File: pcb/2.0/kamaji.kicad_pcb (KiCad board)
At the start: 2 copper layers, 100 x 100 mm, 83 parts, among them J1 RJ10, J2 RJ10, J3 RJ10, J4 RJ10, J5 RJ10, J6 RJ10, J7 USB_B, J8 USB_A, Q1 2N3904, Q2 IRL540N, Q3 IRL540N, SW1 SW_Push, SW2 SW_Push, SW3 SW_Push, U1 ATMEGA32U4-AU, Y1 16MHz

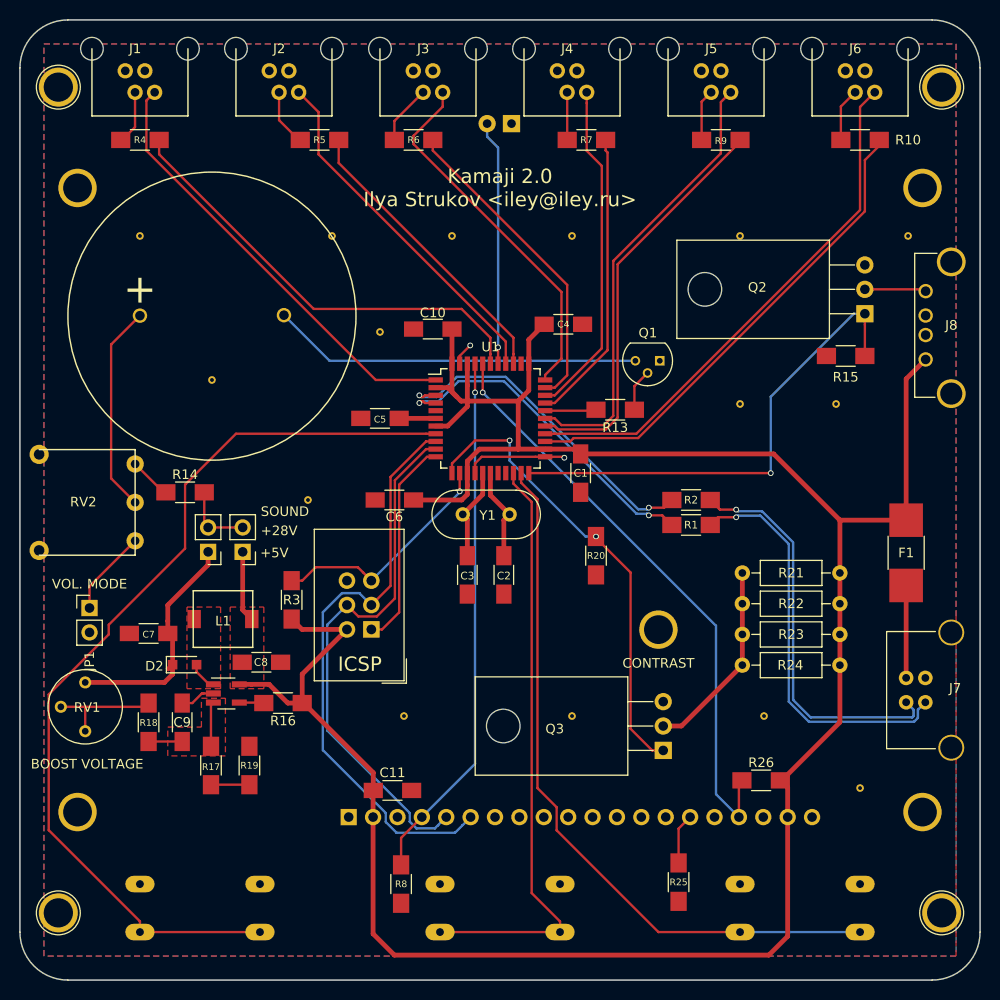
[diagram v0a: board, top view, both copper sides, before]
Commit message: fix a couple of silkscreen labels
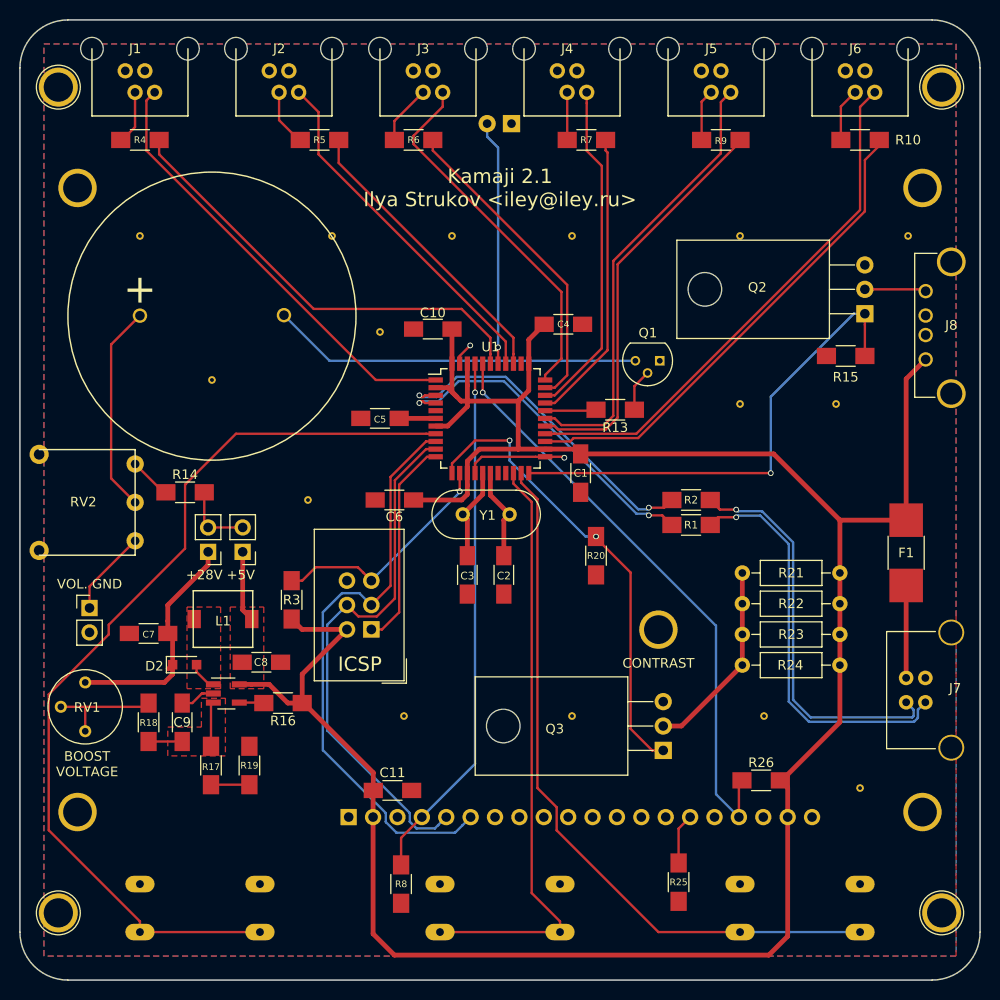
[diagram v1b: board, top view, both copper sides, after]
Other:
- board text added: "Kamaji 2.1 Ilya Strukov <iley@iley.ru>"
- board text added: "VOL. GND"
- board text removed: "Kamaji 2.0 Ilya Strukov <iley@iley.ru>"
- board text removed: "SOUND"
- board text removed: "VOL. MODE"
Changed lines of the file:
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@@
     (area 46.224999 46.55 157.775001 150.075001)
     (thickness 1.6)
-    (drawings 16)
+    (drawings 15)
     (tracks 378)
     (zones 0)
@@
     (descr "Through hole straight pin header, 1x02, 2.54mm pitch, single row")
     (tags "Through hole pin header THT 1x02 2.54mm single row")
-    (fp_text reference JP1 (at 0 5.54 90) (layer F.SilkS)
+    (fp_text reference JP1 (at -2.45 0.95 90) (layer F.SilkS) hide
       (effects (font (size 1 1) (thickness 0.15)))
     )
@@
     (effects (font (size 1 1) (thickness 0.2)))
   )
-  (gr_text "BOOST VOLTAGE" (at 57 127.5) (layer F.SilkS)
+  (gr_text "BOOST\nVOLTAGE" (at 57 127.5) (layer F.SilkS)
     (effects (font (size 1 1) (thickness 0.2)))
   )
-  (gr_text "VOL. MODE" (at 57.25 108.75) (layer F.SilkS)
-    (effects (font (size 1 1) (thickness 0.2)))
-  )
-  (gr_text SOUND (at 77.6 101.2) (layer F.SilkS)
+  (gr_text "VOL. GND" (at 57.25 108.75) (layer F.SilkS)
     (effects (font (size 1 1) (thickness 0.2)))
   )
@@
     (effects (font (size 1.5 1.5) (thickness 0.3)))
   )
-  (gr_text +5V (at 76.5 105.5) (layer F.SilkS)
+  (gr_text +5V (at 73 107.8) (layer F.SilkS)
     (effects (font (size 1 1) (thickness 0.2)))
   )
-  (gr_text +28V (at 77 103.2) (layer F.SilkS)
+  (gr_text +28V (at 69.2 107.8) (layer F.SilkS)
     (effects (font (size 1 1) (thickness 0.2)))
   )
-  (gr_text "Kamaji 2.0\nIlya Strukov <iley@iley.ru>" (at 100 67.5) (layer F.SilkS)
+  (gr_text "Kamaji 2.1\nIlya Strukov <iley@iley.ru>" (at 100 67.5) (layer F.SilkS)
     (effects (font (size 1.5 1.5) (thickness 0.25)))
   )

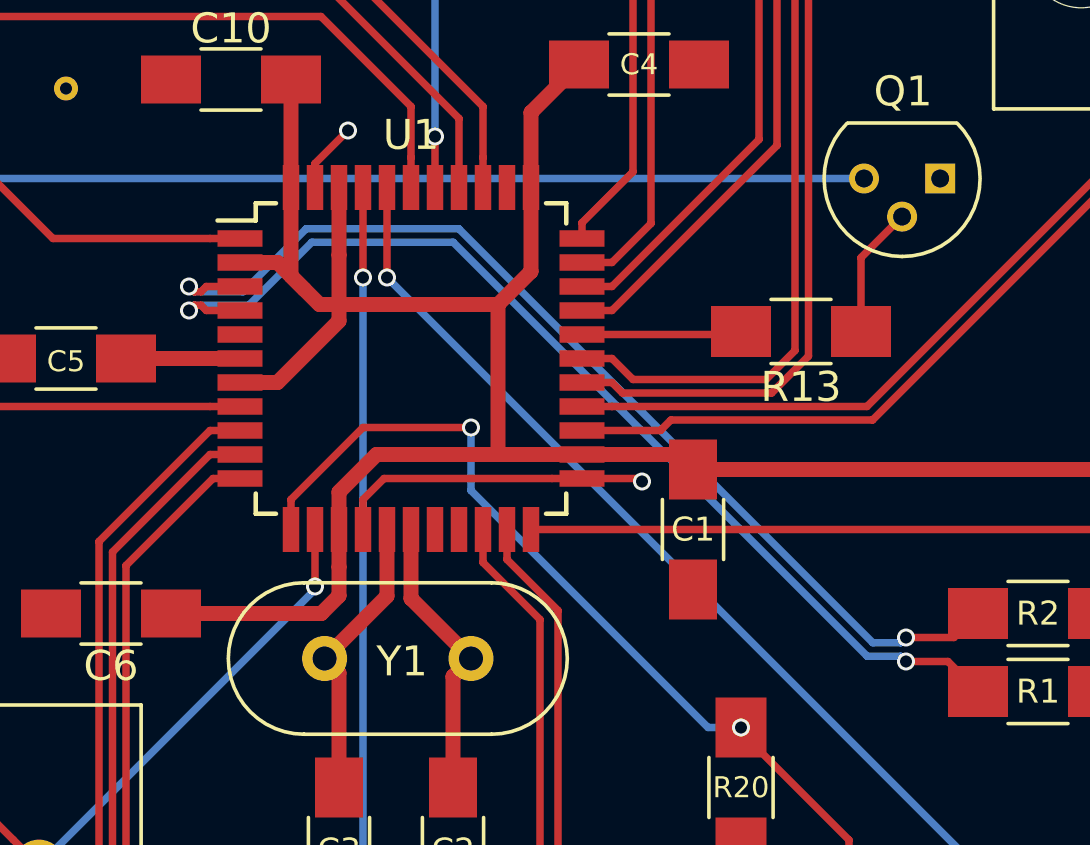
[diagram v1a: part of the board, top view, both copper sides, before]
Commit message: move a couple of tracks
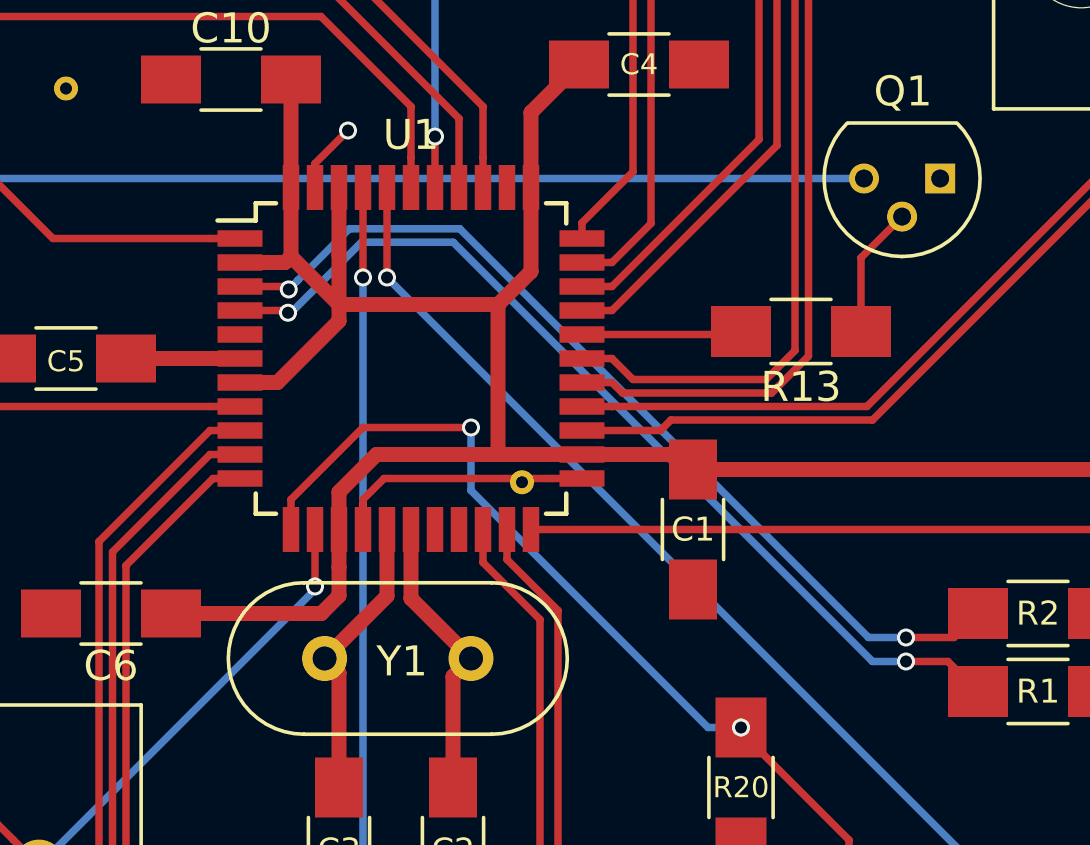
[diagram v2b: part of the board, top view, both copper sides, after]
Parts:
- added VIA**: Via_0.8mm, kamaji:Via_0.8mm, F.Cu at (102.7, 95.6)
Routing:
- net /USB_D-: track 35.2 -> 31.5 mm
- net /USB_D+: track 35.3 -> 31.8 mm
- net GND: track 16.7 -> 14.6 mm, vias 2 -> 1
- net VCC: track 264.2 -> 263.1 mm
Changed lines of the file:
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@@
 (kicad_pcb (version 4) (host pcbnew 4.0.7)
   (general
-    (links 178)
+    (links 179)
     (no_connects 0)
     (area 46.224999 46.55 157.775001 150.075001)
     (thickness 1.6)
     (drawings 15)
-    (tracks 378)
+    (tracks 365)
     (zones 0)
-    (modules 83)
+    (modules 84)
     (nets 57)
   )
@@
   )
   (module kamaji:Via_0.8mm (layer F.Cu)
+    (at 102.7 95.625)
+    (fp_text reference VIA** (at 0 1.5) (layer F.SilkS) hide
+      (effects (font (size 1 1) (thickness 0.15)))
+    )
+    (fp_text value Via_0.8mm (at 0 -1.5) (layer F.Fab) hide
+      (effects (font (size 1 1) (thickness 0.15)))
+    )
+    (pad 1 thru_hole circle (at 0 0) (size 0.8 0.8) (drill 0.4) (layers *.Cu *.Mask)
+      (net 49 GND) (zone_connect 2))
+  )
+  (module kamaji:Via_0.8mm (layer F.Cu)
     (at 80 100)
     (fp_text reference VIA** (at 0 1.5) (layer F.SilkS) hide
@@
   (segment (start 72.85 121.1) (end 75.35 121.1) (width 0.25) (layer F.Cu) (net 2))
   (segment (start 75.35 121.1) (end 75.4 121.15) (width 0.25) (layer F.Cu) (net 2))
+  (segment (start 96.6 89.7) (end 95 88.1) (width 0.5) (layer F.Cu) (net 3))
+  (segment (start 95 88.1) (end 94.8 88.3) (width 0.5) (layer F.Cu) (net 3))
+  (segment (start 94.8 88.3) (end 93.3 88.3) (width 0.5) (layer F.Cu) (net 3))
+  (segment (start 95 88.1) (end 95 85.8) (width 0.5) (layer F.Cu) (net 3))
+  (segment (start 101.9 89.7) (end 96.6 89.7) (width 0.5) (layer F.Cu) (net 3))
   (segment (start 129.961034 133.024284) (end 129.961034 145.438966) (width 0.5) (layer F.Cu) (net 3))
   (segment (start 129.961034 145.438966) (end 128 147.4) (width 0.5) (layer F.Cu) (net 3))
@@
   (segment (start 94.55 92.3) (end 96.6 90.25) (width 0.5) (layer F.Cu) (net 3))
   (segment (start 96.6 90.25) (end 96.6 89.7) (width 0.5) (layer F.Cu) (net 3))
-  (segment (start 101.9 89.7) (end 96.6 89.7) (width 0.5) (layer F.Cu) (net 3))
-  (segment (start 96.6 89.7) (end 95.95 89.7) (width 0.5) (layer F.Cu) (net 3))
-  (segment (start 95.95 89.7) (end 95.45 89.2) (width 0.5) (layer F.Cu) (net 3))
   (segment (start 96.6 99.410002) (end 96.6 98.45) (width 0.5) (layer F.Cu) (net 3))
   (segment (start 96.6 98.45) (end 96.6 97.2) (width 0.5) (layer F.Cu) (net 3))
@@
   (segment (start 103 85.8) (end 103 83.3) (width 0.5) (layer F.Cu) (net 3))
   (segment (start 103 83.3) (end 104.6 81.7) (width 0.5) (layer F.Cu) (net 3))
-  (segment (start 95.45 89.2) (end 95 88.75) (width 0.5) (layer F.Cu) (net 3))
-  (segment (start 95 88.75) (end 95 85.8) (width 0.5) (layer F.Cu) (net 3))
-  (segment (start 94.55 88.3) (end 93.3 88.3) (width 0.5) (layer F.Cu) (net 3))
-  (segment (start 95.45 89.2) (end 94.55 88.3) (width 0.5) (layer F.Cu) (net 3))
   (segment (start 97.85 94.7) (end 96.6 95.95) (width 0.5) (layer F.Cu) (net 3))
   (segment (start 96.6 95.95) (end 96.6 97.2) (width 0.5) (layer F.Cu) (net 3))
@@
   (segment (start 96.6 101.98) (end 96.12 101.5) (width 0.5) (layer F.Cu) (net 5))
   (segment (start 89.5 91.5) (end 93.3 91.5) (width 0.5) (layer F.Cu) (net 6))
-  (via (at 97.4 88.8) (size 0.6) (drill 0.4) (layers F.Cu B.Cu) (net 7))
-  (segment (start 97.4 85.8) (end 97.4 88.8) (width 0.25) (layer F.Cu) (net 7))
-  (segment (start 97.4 127.485318) (end 91.861034 133.024284) (width 0.25) (layer B.Cu) (net 7))
   (segment (start 97.4 88.8) (end 97.4 127.485318) (width 0.25) (layer B.Cu) (net 7))
+  (segment (start 97.4 127.485318) (end 91.861034 133.024284) (width 0.25) (layer B.Cu) (net 7))
+  (segment (start 97.4 85.8) (end 97.4 88.8) (width 0.25) (layer F.Cu) (net 7))
+  (via (at 97.4 88.8) (size 0.6) (drill 0.4) (layers F.Cu B.Cu) (net 7))
   (segment (start 91.861034 133.024284) (end 89.7 135.185318) (width 0.25) (layer F.Cu) (net 7))
   (segment (start 89.7 135.185318) (end 89.7 138) (width 0.25) (layer F.Cu) (net 7))
@@
   (segment (start 118.6 134.225318) (end 119.801034 133.024284) (width 0.25) (layer F.Cu) (net 10))
   (segment (start 98.2 88.8) (end 98.2 85.8) (width 0.25) (layer F.Cu) (net 11))
-  (segment (start 124.881034 133.024284) (end 122.5 130.64325) (width 0.25) (layer B.Cu) (net 11))
-  (segment (start 122.5 130.64325) (end 122.5 113.1) (width 0.25) (layer B.Cu) (net 11))
   (segment (start 122.5 113.1) (end 98.2 88.8) (width 0.25) (layer B.Cu) (net 11))
+  (segment (start 122.5 130.64325) (end 122.5 113.1) (width 0.25) (layer B.Cu) (net 11))
+  (segment (start 124.881034 133.024284) (end 122.5 130.64325) (width 0.25) (layer B.Cu) (net 11))
   (via (at 98.2 88.8) (size 0.6) (drill 0.4) (layers F.Cu B.Cu) (net 11))
   (segment (start 124.881034 133.024284) (end 124.881034 129.518966) (width 0.25) (layer F.Cu) (net 11))
@@
   (segment (start 79.4 108.4) (end 80.8 107) (width 0.25) (layer F.Cu) (net 24))
   (segment (start 80.8 107) (end 85.2 107) (width 0.25) (layer F.Cu) (net 24))
+  (segment (start 96.948072 87.175) (end 95.225065 88.898007) (width 0.25) (layer B.Cu) (net 25))
+  (segment (start 95.225065 88.898007) (end 94.925066 89.198006) (width 0.25) (layer B.Cu) (net 25))
+  (segment (start 100.625 87.175) (end 96.948072 87.175) (width 0.25) (layer B.Cu) (net 25))
+  (segment (start 93.3 89.1) (end 94.82706 89.1) (width 0.25) (layer F.Cu) (net 25))
+  (segment (start 115.5 100.8) (end 114.25 100.8) (width 0.25) (layer B.Cu) (net 25))
+  (segment (start 114.25 100.8) (end 100.625 87.175) (width 0.25) (layer B.Cu) (net 25))
+  (segment (start 94.82706 89.1) (end 94.925066 89.198006) (width 0.25) (layer F.Cu) (net 25))
+  (via (at 94.925066 89.198006) (size 0.6) (drill 0.4) (layers F.Cu B.Cu) (net 25))
   (segment (start 115.5 100.8) (end 117.1 100.8) (width 0.25) (layer F.Cu) (net 25))
-  (segment (start 117.1 100.8) (end 117.9 100) (width 0.25) (layer F.Cu) (net 25))
   (via (at 115.5 100.8) (size 0.6) (drill 0.4) (layers F.Cu B.Cu) (net 25))
-  (segment (start 100.593198 87.175) (end 114.393199 100.975001) (width 0.25) (layer B.Cu) (net 25))
-  (segment (start 114.393199 100.975001) (end 115.324999 100.975001) (width 0.25) (layer B.Cu) (net 25))
-  (segment (start 115.324999 100.975001) (end 115.5 100.8) (width 0.25) (layer B.Cu) (net 25))
-  (segment (start 95.506802 87.175) (end 100.593198 87.175) (width 0.25) (layer B.Cu) (net 25))
-  (segment (start 93.406801 89.275001) (end 95.506802 87.175) (width 0.25) (layer B.Cu) (net 25))
-  (segment (start 91.775001 89.275001) (end 93.406801 89.275001) (width 0.25) (layer B.Cu) (net 25))
-  (segment (start 91.6 89.1) (end 91.775001 89.275001) (width 0.25) (layer B.Cu) (net 25))
-  (segment (start 93.3 89.1) (end 92.175 89.1) (width 0.25) (layer F.Cu) (net 25))
-  (via (at 91.6 89.1) (size 0.6) (drill 0.4) (layers F.Cu B.Cu) (net 25))
-  (segment (start 92.175 89.1) (end 91.999999 89.275001) (width 0.25) (layer F.Cu) (net 25))
-  (segment (start 91.999999 89.275001) (end 91.775001 89.275001) (width 0.25) (layer F.Cu) (net 25))
-  (segment (start 91.775001 89.275001) (end 91.6 89.1) (width 0.25) (layer F.Cu) (net 25))
+  (segment (start 117.1 100.8) (end 117.9 100) (width 0.25) (layer F.Cu) (net 25))
+  (segment (start 115.5 101.6) (end 114.381802 101.6) (width 0.25) (layer B.Cu) (net 26))
+  (segment (start 114.381802 101.6) (end 100.406802 87.625) (width 0.25) (layer B.Cu) (net 26))
+  (segment (start 100.406802 87.625) (end 97.35 87.625) (width 0.25) (layer B.Cu) (net 26))
+  (segment (start 97.35 87.625) (end 95.000006 89.974994) (width 0.25) (layer B.Cu) (net 26))
+  (segment (start 95.000006 89.974994) (end 94.9 89.974994) (width 0.25) (layer B.Cu) (net 26))
+  (segment (start 94.825006 89.9) (end 94.9 89.974994) (width 0.25) (layer F.Cu) (net 26))
+  (via (at 94.9 89.974994) (size 0.6) (drill 0.4) (layers F.Cu B.Cu) (net 26))
+  (segment (start 93.3 89.9) (end 94.825006 89.9) (width 0.25) (layer F.Cu) (net 26))
   (segment (start 115.5 101.6) (end 116.9 101.6) (width 0.25) (layer F.Cu) (net 26))
-  (segment (start 116.9 101.6) (end 117.9 102.6) (width 0.25) (layer F.Cu) (net 26))
   (via (at 115.5 101.6) (size 0.6) (drill 0.4) (layers F.Cu B.Cu) (net 26))
-  (segment (start 100.406802 87.625) (end 114.206801 101.424999) (width 0.25) (layer B.Cu) (net 26))
-  (segment (start 115.324999 101.424999) (end 115.5 101.6) (width 0.25) (layer B.Cu) (net 26))
-  (segment (start 114.206801 101.424999) (end 115.324999 101.424999) (width 0.25) (layer B.Cu) (net 26))
-  (segment (start 95.693198 87.625) (end 100.406802 87.625) (width 0.25) (layer B.Cu) (net 26))
-  (segment (start 93.593199 89.724999) (end 95.693198 87.625) (width 0.25) (layer B.Cu) (net 26))
-  (segment (start 91.6 89.9) (end 91.775001 89.724999) (width 0.25) (layer B.Cu) (net 26))
-  (segment (start 91.775001 89.724999) (end 93.593199 89.724999) (width 0.25) (layer B.Cu) (net 26))
-  (via (at 91.6 89.9) (size 0.6) (drill 0.4) (layers F.Cu B.Cu) (net 26))
-  (segment (start 91.999999 89.724999) (end 91.775001 89.724999) (width 0.25) (layer F.Cu) (net 26))
-  (segment (start 91.775001 89.724999) (end 91.6 89.9) (width 0.25) (layer F.Cu) (net 26))
-  (segment (start 93.3 89.9) (end 92.175 89.9) (width 0.25) (layer F.Cu) (net 26))
-  (segment (start 92.175 89.9) (end 91.999999 89.724999) (width 0.25) (layer F.Cu) (net 26))
+  (segment (start 116.9 101.6) (end 117.9 102.6) (width 0.25) (layer F.Cu) (net 26))
   (segment (start 138 78.06) (end 144.14 78.06) (width 0.25) (layer F.Cu) (net 27))
   (segment (start 144.14 78.06) (end 144.33 78.25) (width 0.25) (layer F.Cu) (net 27))
@@
   (segment (start 138 64.6) (end 139.5 63.1) (width 0.25) (layer F.Cu) (net 48))
   (segment (start 139.5 63.1) (end 139.5 62.5) (width 0.25) (layer F.Cu) (net 48))
-  (segment (start 104.7 95.5) (end 106.6 95.5) (width 0.25) (layer F.Cu) (net 49))
-  (segment (start 106.6 95.5) (end 106.7 95.6) (width 0.25) (layer F.Cu) (net 49))
-  (via (at 106.7 95.6) (size 0.6) (drill 0.4) (layers F.Cu B.Cu) (net 49))
   (segment (start 97.4 97.2) (end 97.4 96.2) (width 0.25) (layer F.Cu) (net 49))
   (segment (start 97.4 96.2) (end 98.1 95.5) (width 0.25) (layer F.Cu) (net 49))
